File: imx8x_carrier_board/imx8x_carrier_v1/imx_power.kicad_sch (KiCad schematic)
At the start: 1 part, among them CN1 DF11-16DP-2DSA(08)

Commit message: IMX8 Board Revisions
Started updating the libraries to be project specific instead of global, that way the project libraries are pushed with it and not lost in translation. WIP
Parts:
- CN1: footprint easyeda2kicad:CONN-TH_DF11-16DP-2DSA-08 -> imx8_carrier_board_footprints:CONN-TH_DF11-16DP-2DSA-08; symbol easyeda2kicad:DF11-16DP-2DSA(08) -> imx8_carrier_board_symbol_library:DF11-16DP-2DSA(08)
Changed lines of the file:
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@@
 	)
 	(symbol
-		(lib_id "easyeda2kicad:DF11-16DP-2DSA(08)")
+		(lib_id "imx8_carrier_board_symbol_library:DF11-16DP-2DSA(08)")
 		(at 54.61 52.07 0)
 		(unit 1)
@@
 			)
 		)
-		(property "Footprint" "easyeda2kicad:CONN-TH_DF11-16DP-2DSA-08"
+		(property "Footprint" "imx8_carrier_board_footprints:CONN-TH_DF11-16DP-2DSA-08"
 			(at 54.61 68.58 0)
 			(effects

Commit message: Schematic Updates
WIP.
SOM Connector global labels have been updated.
Commit to update remote. Disregard.
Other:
- note added: "IMX8X Primary Power Input"
- moved on the sheet: CN1
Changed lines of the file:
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@@
 	(generator_version "9.0")
 	(paper "A4")
+	(text "IMX8X Primary Power Input"
+		(exclude_from_sim no)
+		(at 35.56 15.875 0)
+		(effects
+			(font
+				(size 2.032 2.032)
+				(thickness 0.4064)
+				(bold yes)
+			)
+		)
+	)
+	(text_box "Input power comes from the SCALES EPS board, this power connector must also include the necessary I2C lines that connect the monitoring INA260 IC's to the IMX8X"
+		(exclude_from_sim no)
+		(at 13.97 19.05 0)
+		(size 56.515 11.43)
+		(margins 0.9525 0.9525 0.9525 0.9525)
+		(stroke
+			(width 0)
+			(type solid)
+		)
+		(fill
+			(type none)
+		)
+		(effects
+			(font
+				(size 1.27 1.27)
+				(thickness 0.254)
+				(bold yes)
+			)
+			(justify left top)
+		)
+	)
 	(symbol
 		(lib_id "power:GND")
@@
 	(symbol
 		(lib_id "imx8_carrier_board_symbol_library:DF11-16DP-2DSA(08)")
-		(at 54.61 52.07 0)
+		(at 78.105 65.405 0)
 		(unit 1)
 		(exclude_from_sim no)
@@
 		(fields_autoplaced yes)
 		(property "Reference" "CN1"
-			(at 54.61 35.56 0)
+			(at 78.105 48.895 0)
 			(effects
 				(font
@@
 		)
 		(property "Value" "DF11-16DP-2DSA(08)"
-			(at 54.61 38.1 0)
+			(at 78.105 51.435 0)
 			(effects
 				(font
@@
 		)
 		(property "Footprint" "imx8_carrier_board_footprints:CONN-TH_DF11-16DP-2DSA-08"
-			(at 54.61 68.58 0)
+			(at 78.105 81.915 0)
 			(effects
 				(font
@@
 		)
 		(property "Datasheet" "https://lcsc.com/product-detail/Wire-To-Board-Wire-To-Wire-Connector_HRS-Hirose-HRS-DF11-16DP-2DSA-08_C530981.html"
-			(at 54.61 71.12 0)
+			(at 78.105 84.455 0)
 			(effects
 				(font
@@
 		)
 		(property "Description" ""
-			(at 54.61 52.07 0)
+			(at 78.105 65.405 0)
 			(effects
 				(font
@@
 		)
 		(property "LCSC Part" "C530981"
-			(at 54.61 73.66 0)
-			(effects
-				(font
+			(at 78.105 86.995 0)
+			(effects
+				(font

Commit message: Updated Schematic
Working on Micro SD card connector.
Working on implementing power connector. Still uncertain about some things I still need to implement. WIP
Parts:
- added TP10, TP11, TP9: TestPoint, symbol Connector:TestPoint
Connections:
- net GND: now also CN1.11, CN1.13, CN1.15, CN1.9
- net VCC_3V3: now also CN1.1, CN1.3, CN1.5, CN1.7
- net at CN1.10: now also TP11.1
- net SCU_WDOG0_WDOG_OUT: now reaches CN1.16
- net at CN1.2: now also TP9.1
- net at CN1.4: now also TP10.1
- net ADMA_I2C0_SDA: now reaches CN1.6
- net ADMA_I2C0_SCL: now reaches CN1.8
- no-connect marks 0 -> 2
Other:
- note added: "DF11 Power Connector"
- moved on the sheet: CN1

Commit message: Schematic Updates
WIP
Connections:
- net ADMA_I2C0_SCL renamed X_ADMA_I2C0_SCL
- net ADMA_I2C0_SDA renamed X_ADMA_I2C0_SDA
- net SCU_WDOG0_WDOG_OUT renamed X_SCU_WDOG0_WDOG_OUT
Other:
- moved on the sheet: CN1, TP10, TP11, TP9

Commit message: Schematic Updates
WIP
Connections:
- net X_LSIO_GPIO2_IO00: now reaches CN1.12
- net X_LSIO_GPIO2_IO03: now reaches CN1.14
- no-connect marks 2 -> 0
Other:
- moved on the sheet: CN1, TP10, TP11, TP9

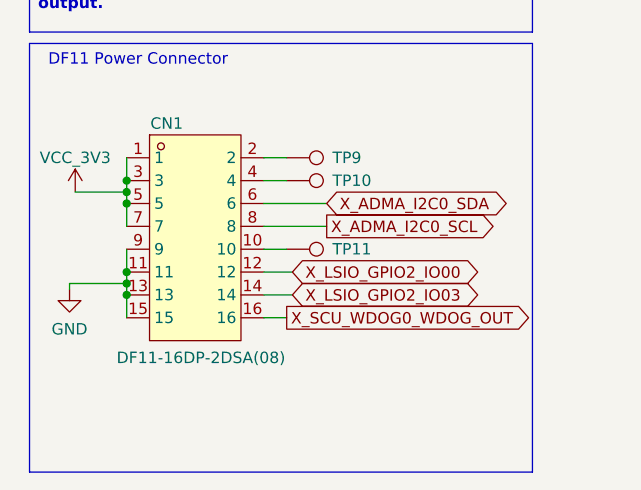
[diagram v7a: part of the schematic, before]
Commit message: Update to Schematic
Did some overview of the schematic and did some touch ups. There are still some GPIOs that need to wired to pins.
All signals should be named correctly and connected the same.

Will need a document review before PCB layout.
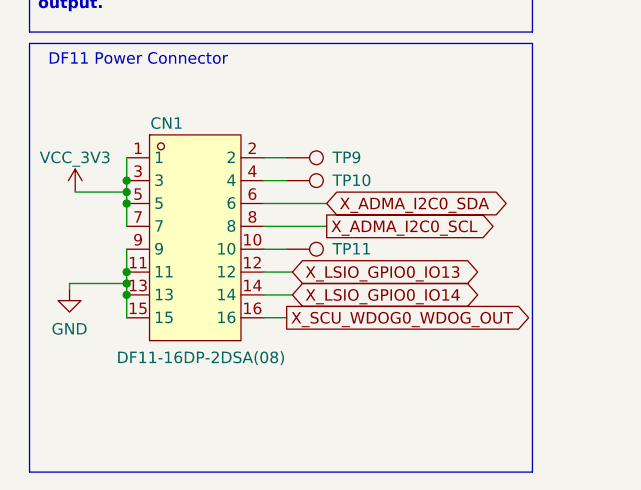
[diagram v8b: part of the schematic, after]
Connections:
- net X_LSIO_GPIO2_IO00 renamed X_LSIO_GPIO0_IO13
- net X_LSIO_GPIO2_IO03 renamed X_LSIO_GPIO0_IO14
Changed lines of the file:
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@@
 		)
 	)
-	(global_label "X_LSIO_GPIO2_IO00"
+	(global_label "X_LSIO_GPIO0_IO13"
 		(shape bidirectional)
 		(at 43.815 84.455 0)
@@
 		)
 	)
-	(global_label "X_LSIO_GPIO2_IO03"
+	(global_label "X_LSIO_GPIO0_IO14"
 		(shape bidirectional)
 		(at 43.815 86.995 0)
